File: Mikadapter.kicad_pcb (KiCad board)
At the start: 2 copper layers, 40.6 x 41.9 mm, 11 parts, among them J1 RJ45, J2 Conn_01x03_Female, J3 RJ45, J4 Conn_01x03_Female, J5 Conn_01x02_Female, J6 Conn_01x03_Female, J7 Conn_01x02_Female

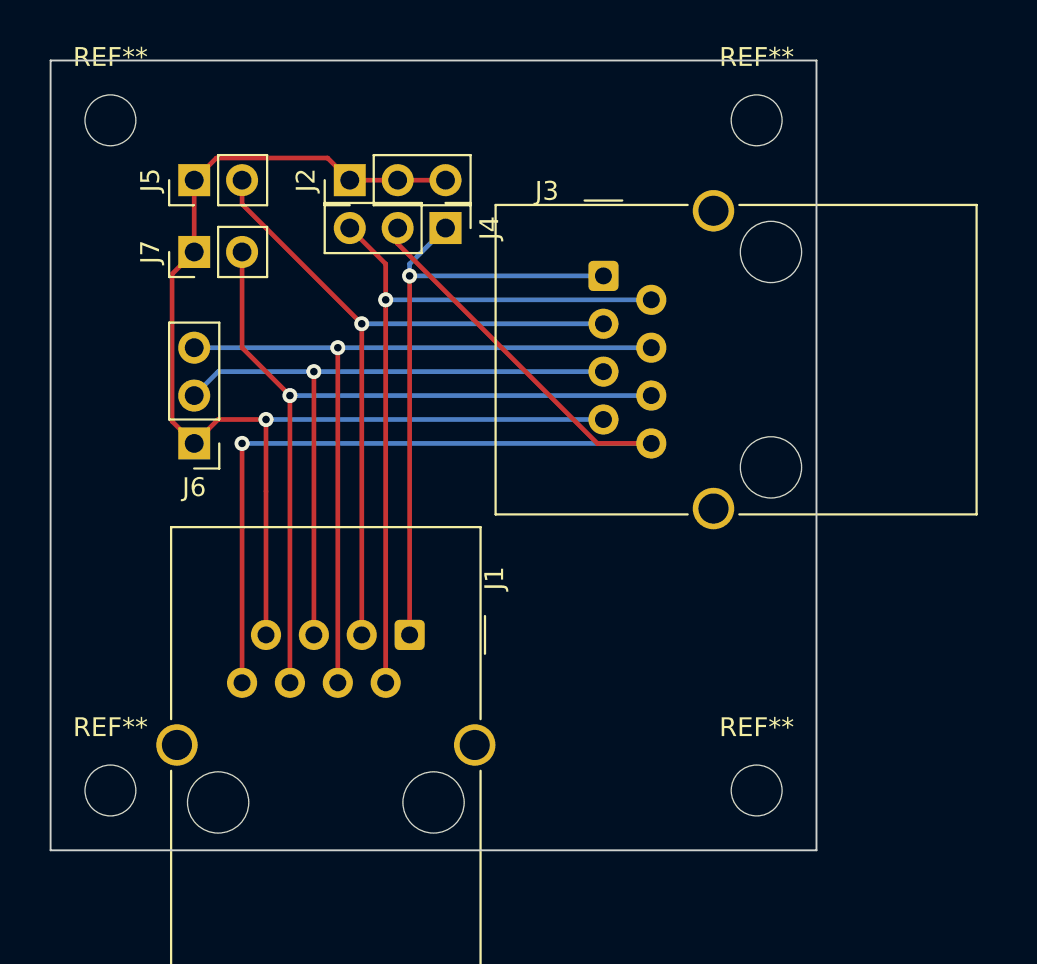
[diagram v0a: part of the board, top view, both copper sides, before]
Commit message: changed width of 5V trace and pinout on the sides
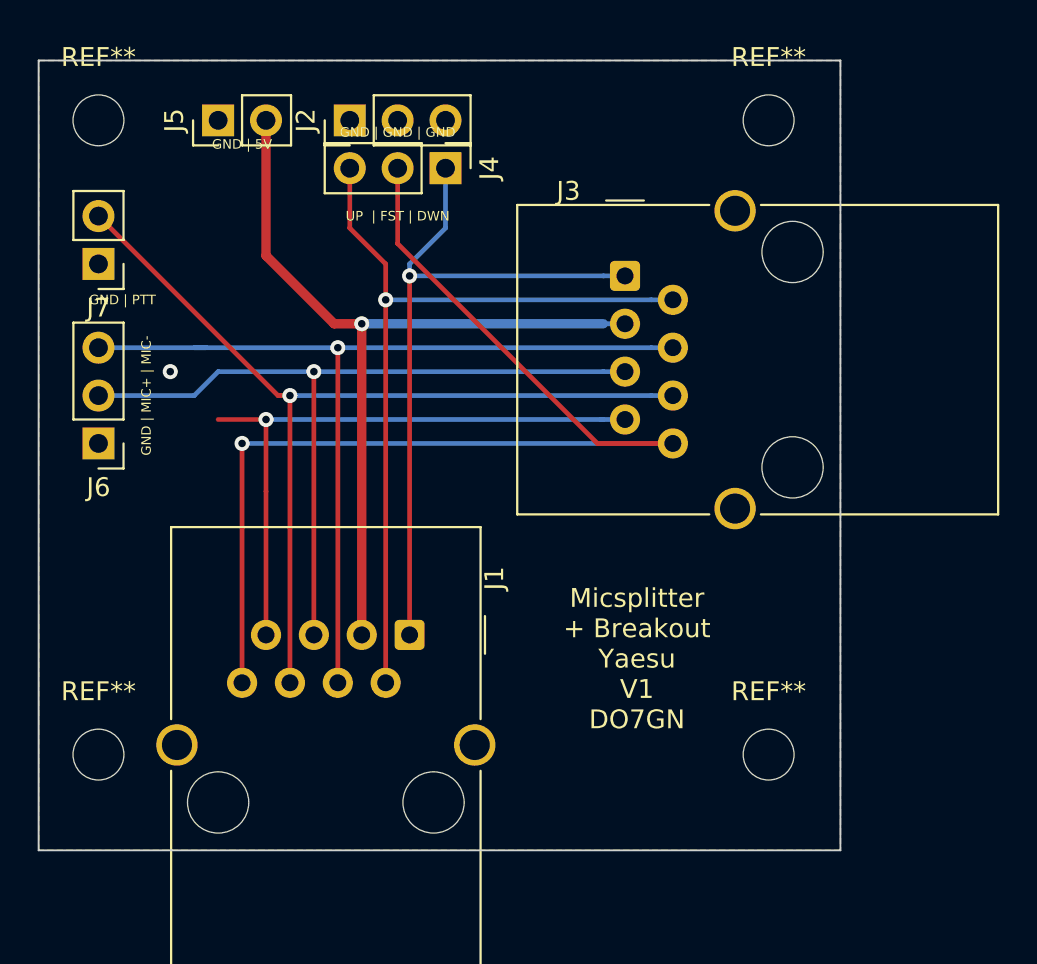
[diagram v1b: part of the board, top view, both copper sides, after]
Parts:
- removed the REF** at (128.3, 83.2)
- removed the REF** at (162.6, 83.2)
- removed the REF** at (128.3, 47.6)
- added REF**: MountingHole_2.7mm_M2.5_DIN965, MountingHole:MountingHole_2.7mm_M2.5_DIN965, F.Cu at (163.2, 81.3)
- added REF**: MountingHole_2.7mm_M2.5_DIN965, MountingHole:MountingHole_2.7mm_M2.5_DIN965, F.Cu at (127.6, 81.3)
- added REF**: MountingHole_2.7mm_M2.5_DIN965, MountingHole:MountingHole_2.7mm_M2.5_DIN965, F.Cu at (127.6, 47.6)
- moved J7 5.12 mm to (127.6, 55.2), turned to 180 degrees
- moved J6 5.08 mm to (127.6, 64.8)
- moved J5 3.42 mm to (134.0, 47.6)
- moved J4 3.18 mm to (146.1, 50.2)
- moved J2 3.17 mm to (141.0, 47.6)
- moved J3 1.14 mm to (155.6, 55.9)
- moved REF** 0.63 mm to (163.2, 47.6)
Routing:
- net GND: track 62.9 -> 33.1 mm, vias 1 -> 2
- net PTT: track 43.1 -> 50.2 mm
- net MIC-: track 42.0 -> 48.9 mm
- net MIC+: track 36.2 -> 42.4 mm
- net FST: track 53.1 -> 58.6 mm
- net 5V: track 39.6 -> 44.2 mm
- net UP: track 39.0 -> 43.3 mm
- net DWN: track 33.3 -> 37.0 mm
- added copper zone on B.Cu, net GND
- added copper zone on F.Cu, net GND
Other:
- board size 40.6 x 41.9 mm -> 42.5 x 41.9 mm
- board text added: "GND | 5V"
- board text added: "GND | GND | GND"
- board text added: "GND | MIC+ | MIC-"
- board text added: "GND | PTT"
- board text added: "Micsplitter + Breakout Yaesu V1 DO7GN"
- board text added: "UP | FST | DWN"

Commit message: changed layout for FST|DWN|UP buttons
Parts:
- removed J4: Conn_01x03_Female, Connector_PinHeader_2.54mm:PinHeader_1x03_P2.54mm_Vertical
- J2: value Conn_01x03_Female -> Conn_01x04_Female; footprint Connector_PinHeader_2.54mm:PinHeader_1x03_P2.54mm_Vertical -> Connector_PinHeader_2.54mm:PinHeader_1x04_P2.54mm_Vertical
- moved J2 7.62 mm to (148.6, 47.6), turned to 270 degrees
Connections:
- J2 pad 2: GND -> DWN
- J2 pad 3: GND -> FST
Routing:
- net FST: track 58.6 -> 61.1 mm
- net UP: track 43.3 -> 45.9 mm
- net DWN: track 37.0 -> 39.5 mm
- net GND: vias 2 -> 3

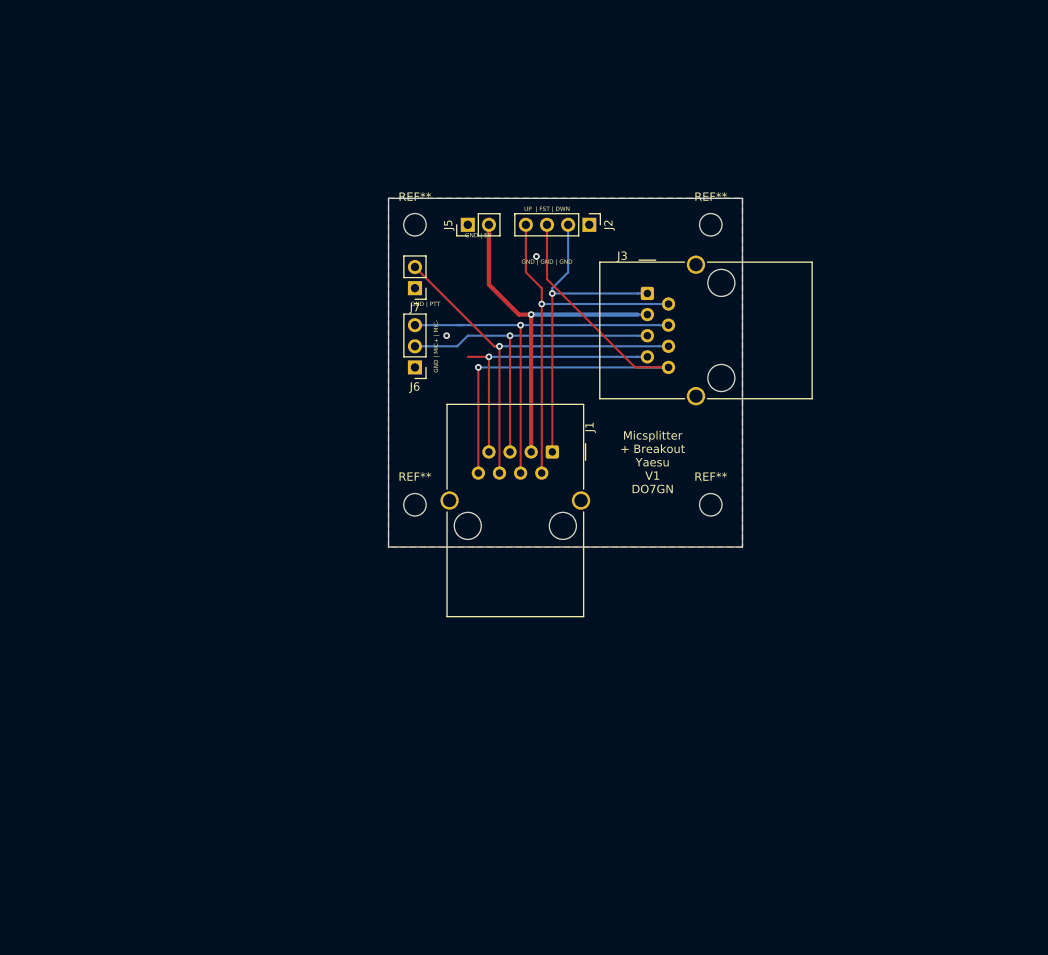
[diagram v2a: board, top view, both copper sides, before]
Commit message: transformed in KiCAD 6 and changed layout and changed pinout for RJ45
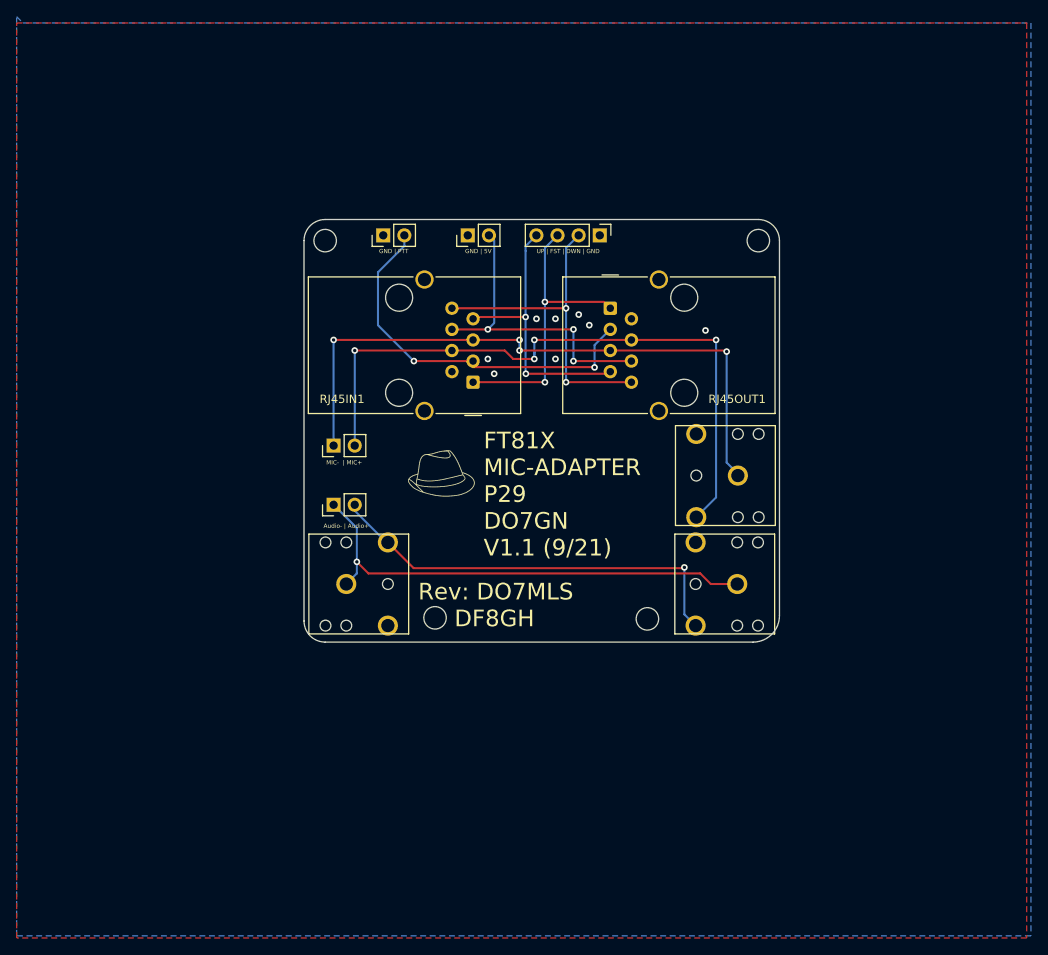
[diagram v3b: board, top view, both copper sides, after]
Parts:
- removed the REF** at (163.2, 81.3)
- removed the REF** at (127.6, 81.3)
- removed the REF** at (127.6, 47.6)
- added G***: LOGO, Fedora:FedoraDO7GN, F.Cu at (130.8, 77.5)
- added J3: FC68131, Addtional_DO7GN:CLIFF_FC68131, F.Cu at (166.4, 90.8)
- added J4: FC68131, Addtional_DO7GN:CLIFF_FC68131, F.Cu at (119.4, 90.8)
- added J9: Conn_01x03_Female, Connector_PinHeader_2.54mm:PinHeader_1x02_P2.54mm_Vertical, F.Cu at (117.9, 81.3)
- added REF**: MountingHole_2.7mm_M2.5_DIN965, MountingHole:MountingHole_2.7mm_M2.5_DIN965, F.Cu at (155.6, 95.0)
- added REF**: MountingHole_2.7mm_M2.5_DIN965, MountingHole:MountingHole_2.7mm_M2.5_DIN965, F.Cu at (130.0, 94.9)
- added REF**: MountingHole_2.7mm_M2.5_DIN965, MountingHole:MountingHole_2.7mm_M2.5_DIN965, F.Cu at (116.8, 49.5)
- added REF**: KiCad-Logo_5mm_SilkScreen, Symbol:KiCad-Logo_5mm_SilkScreen, B.Cu at (149.9, 81.0)
- added RJ45IN1: RJ45, Connector_RJ:RJ45_Wuerth_7499010001A_Horizontal, F.Cu at (134.6, 66.5)
- added e: OSHW-Logo2_7.3x6mm_SilkScreen, Symbol:OSHW-Logo2_7.3x6mm_SilkScreen, B.Cu at (137.2, 81.3)
- J1: value RJ45 -> FC68131; footprint Connector_RJ:RJ45_Wuerth_7499010001A_Horizontal -> Addtional_DO7GN:CLIFF_FC68131
- J6: footprint Connector_PinHeader_2.54mm:PinHeader_1x03_P2.54mm_Vertical -> Connector_PinHeader_2.54mm:PinHeader_1x02_P2.54mm_Vertical
- RJ45OUT1: renamed from J3; value RJ45 -> RJ45OUT
- moved J1 22.5 mm to (166.4, 77.8), turned to 180 degrees
- moved J6 13.6 mm to (117.9, 74.2), turned to 90 degrees
- moved J7 7.41 mm to (123.8, 48.9), turned to 90 degrees
- moved REF** 6.02 mm to (168.9, 49.5)
- moved RJ45OUT1 4.80 mm to (151.1, 57.7)
- moved J2 1.79 mm to (149.8, 48.9)
- moved J5 1.27 mm to (134.0, 48.9)
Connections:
- J1 pad 1: DWN -> MIC-
- J1 pad 2: UP -> MIC+
- J1 pad 5: MIC+ -> unconnected-(J1-Pad5)
- J6 pad 1: GND -> MIC-
- RJ45OUT1 pad 1: DWN -> FST
- RJ45OUT1 pad 2: UP -> GND
- RJ45OUT1 pad 3: 5V -> PTT
- RJ45OUT1 pad 4: MIC- -> MIC+
- RJ45OUT1 pad 5: MIC+ -> MIC-
- RJ45OUT1 pad 6: PTT -> 5V
- RJ45OUT1 pad 7: GND -> UP
- RJ45OUT1 pad 8: FST -> DWN
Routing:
- net Audio-: track 0.00 -> 58.0 mm, vias 0 -> 1
- net Audio+: track 0.00 -> 50.9 mm, vias 0 -> 1
- net MIC+: track 42.4 -> 80.1 mm, vias 1 -> 4
- net GND: track 33.1 -> 0.00 mm, vias 3 -> 8
- net MIC-: track 48.9 -> 76.7 mm, vias 1 -> 4
- net FST: track 61.1 -> 35.1 mm, vias 1 -> 2
- net UP: track 45.9 -> 34.3 mm, vias 1 -> 2
- net 5V: track 44.2 -> 37.1 mm, vias 1 -> 3
- net PTT: track 50.2 -> 45.6 mm, vias 1 -> 2
- net DWN: track 39.5 -> 39.9 mm, vias 1 -> 2
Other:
- board size 42.5 x 41.9 mm -> 57.1 x 50.8 mm
- net class Default removed
- rule pad_to_mask_clearance: 0.051 -> 0
- board text added: "Audio- | Audio+"
- board text added: "FT81X MIC-ADAPTER P29 DO7GN V1.1 (9/21)"
- board text added: "MIC- | MIC+"
- board text added: "Rev: DO7MLS DF8GH"
- board text added: "UP | FST | DWN | GND"
- board text removed: "GND | GND | GND"
- board text removed: "GND | MIC+ | MIC-"
- board text removed: "Micsplitter + Breakout Yaesu V1 DO7GN"
- board text removed: "UP | FST | DWN"

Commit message: changed name to ft-81x
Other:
- board text added: "FT-81X MIC-ADAPTER P29 DO7GN V1.1 (9/21)"
- board text removed: "FT81X MIC-ADAPTER P29 DO7GN V1.1 (9/21)"
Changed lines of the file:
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@@
     (effects (font (size 0.508 0.508) (thickness 0.127)))
   )
-  (gr_text "FT81X\nMIC-ADAPTER\nP29\nDO7GN\nV1.1 (9/21)" (at 135.89 80.01) (layer "F.SilkS")
+  (gr_text "FT-81X\nMIC-ADAPTER\nP29\nDO7GN\nV1.1 (9/21)" (at 135.89 80.01) (layer "F.SilkS")
     (effects (font (size 2 2) (thickness 0.3)) (justify left))
   )

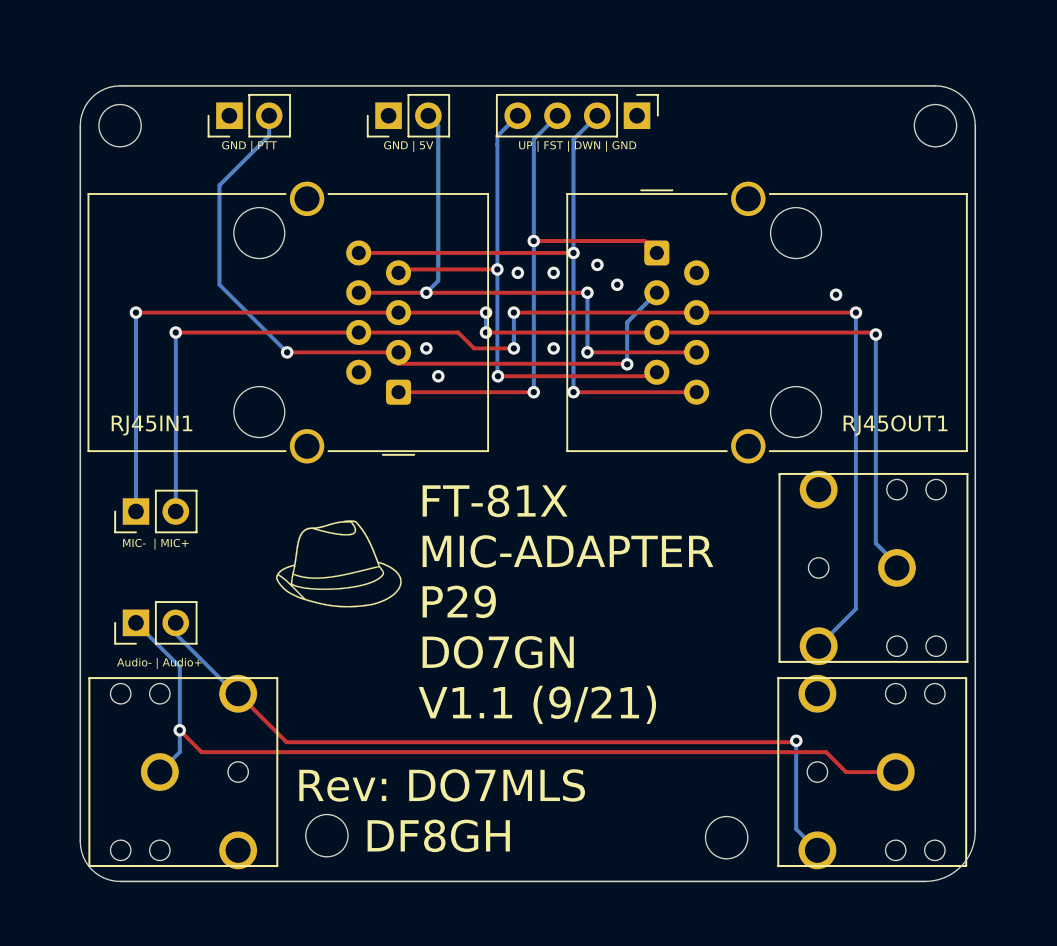
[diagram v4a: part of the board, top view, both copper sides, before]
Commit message: Changed Audio pins after inspection of the jack
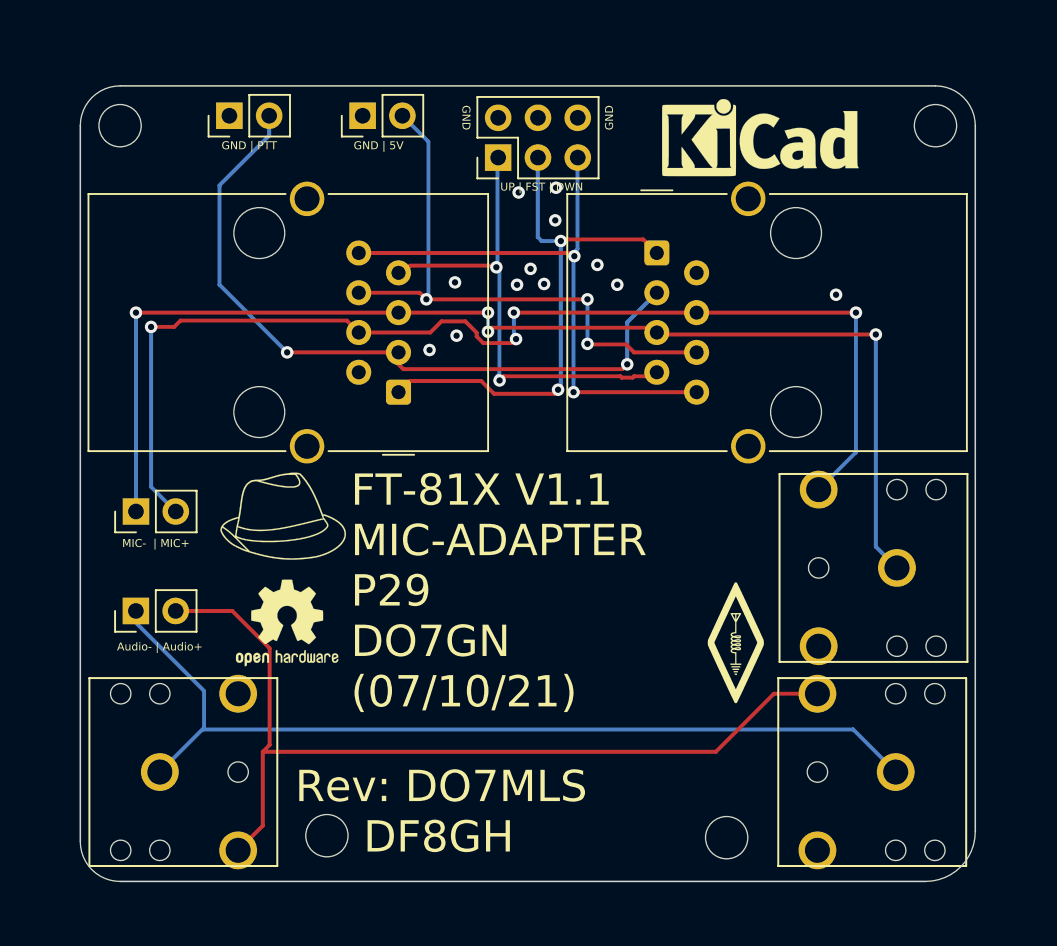
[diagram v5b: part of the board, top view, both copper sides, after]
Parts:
- removed J2: Conn_01x04_Female, Connector_PinHeader_2.54mm:PinHeader_1x04_P2.54mm_Vertical
- added G***: LOGO, LOGO, F.Cu at (156.2, 82.5)
- added J8: Conn_01x04_Female, Connector_PinHeader_2.54mm:PinHeader_2x03_P2.54mm_Vertical, F.Cu at (141.0, 51.6)
- REF**, e: moved to F.Cu
- moved REF** 31.2 mm to (157.7, 50.8), turned to 0 degrees
- moved e 9.65 mm to (127.5, 81.3), turned to 0 degrees
- moved G*** 4.68 mm to (127.3, 74.4)
- moved J5 1.66 mm to (132.3, 48.9)
- moved J9 0.76 mm to (117.9, 80.5)
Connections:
- J1 pad 2: MIC+ -> unconnected-(J1-Pad2)
- J1 pad 5: unconnected-(J1-Pad5) -> MIC+
- J3 pad 2: Audio+ -> unconnected-(J3-Pad2)
- J3 pad 5: unconnected-(J3-Pad5) -> Audio+
- J4 pad 2: Audio+ -> unconnected-(J4-Pad2)
- J4 pad 5: unconnected-(J4-Pad5) -> Audio+
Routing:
- net Audio+: track 50.9 -> 57.7 mm, vias 1 -> 0
- net MIC+: track 80.1 -> 73.5 mm
- net DWN: track 39.9 -> 37.1 mm
- net UP: track 34.3 -> 31.5 mm
- net FST: track 35.1 -> 33.9 mm
- net Audio-: track 58.0 -> 57.9 mm, vias 1 -> 0
- net GND: vias 8 -> 12
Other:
- board text added: "FT-81X V1.1 MIC-ADAPTER P29 DO7GN (07/10/21)"
- board text added: "GND"
- board text added: "UP | FST | DWN"
- board text removed: "FT-81X MIC-ADAPTER P29 DO7GN V1.1 (9/21)"
- board text removed: "UP | FST | DWN | GND"
